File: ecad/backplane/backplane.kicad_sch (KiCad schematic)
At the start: 18 parts, among them J1 10145891-0320J13LF, J2 10145891-0320J13LF, J3 10145891-0320J13LF, J4 10145891-0320J13LF, J6 USB4105-GF-A, U1 MCP16331x-xCH

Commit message: hii
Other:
- moved on the sheet: R3, R4

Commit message: fix backplane pins
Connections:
- net ADDR01 is gone; now on net GND: J1.3, J2.3, J3.3, J4.3
- net ADDR03 is gone; now on net GND: J1.4, J2.4, J3.4, J4.4
- net ADDR05 is gone; now on net BUS05: J1.5, J2.5, J3.5, J4.5
- net ADDR07 is gone; now on net BUS06: J1.6, J2.6, J3.6, J4.6
- net ADDR09 is gone; now on net BUS09: J1.9, J2.9, J3.9, J4.9
- net ADDR10 is gone; now on net 3.3V: J1.49, J2.49, J3.49, J4.49
- net ADDR11 is gone; now on net BUS10: J1.10, J2.10, J3.10, J4.10
- net ADDR12 is gone; now on net 3.3V: J1.50, J2.50, J3.50, J4.50
- net ADDR13 is gone; now on net BUS11: J1.11, J2.11, J3.11, J4.11
- net ADDR14 is gone; now on net GND: J1.51, J2.51, J3.51, J4.51
- net ADDR15 is gone; now on net BUS12: J1.12, J2.12, J3.12, J4.12
- net BUS01 is gone; now on net GND: J1.15, J2.15, J3.15, J4.15
- net BUS03 is gone; now on net GND: J1.16, J2.16, J3.16, J4.16
- net BUS13 is gone; now on net BUS23: J1.23, J2.23, J3.23, J4.23
- net BUS14 is gone; now on net GND: J1.63, J2.63, J3.63, J4.63
- net DATA02 is gone; now on net 3.3V: J1.73, J2.73, J3.73, J4.73
- net DATA04 is gone; now on net 3.3V: J1.74, J2.74, J3.74, J4.74
- net DATA06 is gone; now on net GND: J1.75, J2.75, J3.75, J4.75
- net 3.3V: now also J1.14, J1.2, J1.26, J1.38, J1.61, J1.62, J2.14, J2.2, J2.26, J2.38, J2.61, J2.62, J3.14, J3.2, J3.26, J3.38, J3.61, J3.62, J4.14, J4.2, J4.26, J4.38, J4.61, J4.62; no longer J1.19, J1.31, J1.40, J1.46, J1.52, J1.58, J1.64, J1.7, J1.70, J1.76, J2.19, J2.31, J2.40, J2.46, J2.52, J2.58, J2.64, J2.7, J2.70, J2.76, J3.19, J3.31, J3.40, J3.46, J3.52, J3.58, J3.64, J3.7, J3.70, J3.76, J4.19, J4.31, J4.40, J4.46, J4.52, J4.58, J4.64, J4.7, J4.70, J4.76
- net BUS05: no longer J1.17, J2.17, J3.17, J4.17
- net BUS06: no longer J1.57, J2.57, J3.57, J4.57
- net BUS07: now also J1.7, J2.7, J3.7, J4.7; no longer J1.18, J2.18, J3.18, J4.18
- net BUS08: now also J1.8, J2.8, J3.8, J4.8; no longer J1.60, J2.60, J3.60, J4.60
- net BUS09: no longer J1.21, J2.21, J3.21, J4.21
- net BUS10: no longer J1.61, J2.61, J3.61, J4.61
- net BUS11: no longer J1.22, J2.22, J3.22, J4.22
- net BUS12: no longer J1.62, J2.62, J3.62, J4.62
- net BUS17: now also J1.17, J2.17, J3.17, J4.17; no longer J1.27, J2.27, J3.27, J4.27
- net BUS18: now also J1.18, J2.18, J3.18, J4.18; no longer J1.67, J2.67, J3.67, J4.67
- net BUS19: now also J1.19, J2.19, J3.19, J4.19; no longer J1.28, J2.28, J3.28, J4.28
- net BUS20: now also J1.20, J2.20, J3.20, J4.20; no longer J1.68, J2.68, J3.68, J4.68
- net BUS21: now also J1.21, J2.21, J3.21, J4.21; no longer J1.29, J2.29, J3.29, J4.29
- net BUS22: now also J1.22, J2.22, J3.22, J4.22; no longer J1.69, J2.69, J3.69, J4.69
- net BUS23: no longer J1.30, J2.30, J3.30, J4.30
- net GND: now also J1.27, J1.28, J1.39, J1.40, J1.52, J1.64, J1.76, J2.27, J2.28, J2.39, J2.40, J2.52, J2.64, J2.76, J3.27, J3.28, J3.39, J3.40, J3.52, J3.64, J3.76, J4.27, J4.28, J4.39, J4.40, J4.52, J4.64, J4.76; no longer J1.14, J1.2, J1.20, J1.26, J1.32, J1.38, J1.41, J1.47, J1.53, J1.59, J1.65, J1.71, J1.77, J1.8, J2.14, J2.2, J2.20, J2.26, J2.32, J2.38, J2.41, J2.47, J2.53, J2.59, J2.65, J2.71, J2.77, J2.8, J3.14, J3.2, J3.20, J3.26, J3.32, J3.38, J3.41, J3.47, J3.53, J3.59, J3.65, J3.71, J3.77, J3.8, J4.14, J4.2, J4.20, J4.26, J4.32, J4.38, J4.41, J4.47, J4.53, J4.59, J4.65, J4.71, J4.77, J4.8
- net ADDR00 renamed BUS42
- net ADDR02 renamed BUS43
- net ADDR04 renamed BUS44
- net ADDR06 renamed BUS45
- net ADDR08 renamed BUS48
- net BUS00 renamed BUS54
- net BUS02 renamed BUS55
- net BUS04 renamed BUS56
- net BUS15 renamed BUS24
- net BUS16 renamed BUS66
- net DATA00 renamed BUS72
- net DATA01 renamed BUS33
- net DATA03 renamed BUS34
- net DATA05 renamed BUS35
- net DATA07 renamed BUS36
- new net BUS29: J1.29, J2.29, J3.29, J4.29
- new net BUS30: J1.30, J2.30, J3.30, J4.30
- new net BUS31: J1.31, J2.31, J3.31, J4.31
- new net BUS32: J1.32, J2.32, J3.32, J4.32
- new net BUS41: J1.41, J2.41, J3.41, J4.41
- new net BUS46: J1.46, J2.46, J3.46, J4.46
- new net BUS47: J1.47, J2.47, J3.47, J4.47
- new net BUS53: J1.53, J2.53, J3.53, J4.53
- new net BUS57: J1.57, J2.57, J3.57, J4.57
- new net BUS58: J1.58, J2.58, J3.58, J4.58
- new net BUS59: J1.59, J2.59, J3.59, J4.59
- new net BUS60: J1.60, J2.60, J3.60, J4.60
- new net BUS65: J1.65, J2.65, J3.65, J4.65
- new net BUS67: J1.67, J2.67, J3.67, J4.67
- new net BUS68: J1.68, J2.68, J3.68, J4.68
- new net BUS69: J1.69, J2.69, J3.69, J4.69
- new net BUS70: J1.70, J2.70, J3.70, J4.70
- new net BUS71: J1.71, J2.71, J3.71, J4.71
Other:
- note added: "Buck Converter"

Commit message: more backplane. add nathan's panel changes
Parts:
- added J6: 5017868090, Library:CON_5017868090, symbol Project_Library:5017868090
- added S1: 500SSP1S1M7QEA, Library:SW_500SSP1S1M7QEA, symbol Project_Library:500SSP1S1M7QEA
- renumbered C4 to C1, C5 to C2, C2 to CB1, C1 to Cln_1, C6 to Cln_2, D2 to D1, D1 to DB1, J3 to J2, J6 to J3, J2 to J4, J4 to J5, R3 to R1, R4 to R2, R2 to RBot1, R1 to RTop1
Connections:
- net 3.3V: now also S1.1; no longer C1.1, C2.1, DB1.2 (A), L1.2, RTop1.2
- new net 3.3V IN: C1.1, C2.1, DB1.2 (A), L1.2, RTop1.2, S1.2
- no-connect marks 855 -> 856
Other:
- note added: "Power on"
- note added: "add protection diode"

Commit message: backplane with addr
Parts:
- added R3: 10, Resistor_SMD:R_0402_1005Metric_Pad0.72x0.64mm_HandSolder, symbol Device:R_US
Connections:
- net 3.3V IN: now also R3.2; no longer RTop1.2
- net at J3.A5 (CC1): now also R2.1
- net at J3.B5 (CC2): now also R1.1
- net at J3.B6 (DP2): no longer R2.1
- net at J3.B7 (DN2): no longer R1.1
- net at U1.1 (BOOST): now also CB1.1, DB1.1 (K); no longer CB1.2
- net at D1.1 (K), L1.1, U1.6 (SW): now also CB1.2
- net +5V renamed VBUS
- new net: R3.1, RTop1.2
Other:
- moved on the sheet: CB1

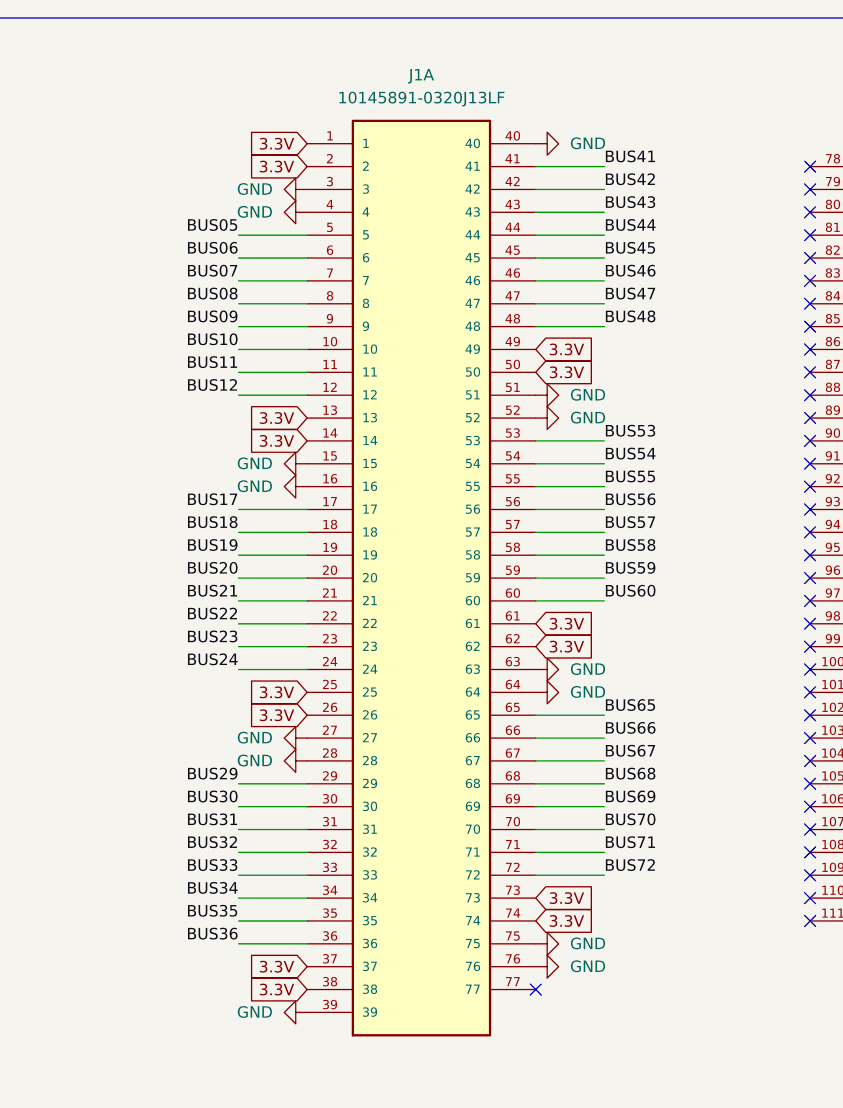
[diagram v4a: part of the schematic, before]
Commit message: backplane with different bus names
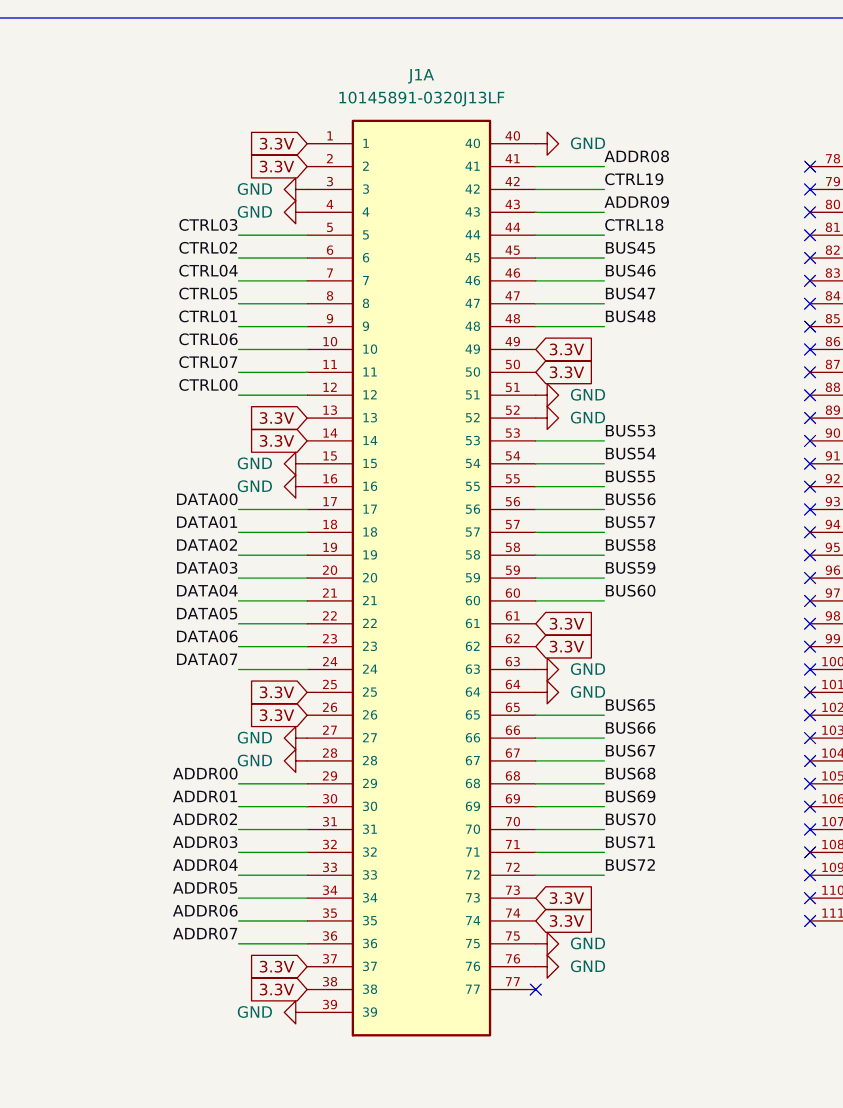
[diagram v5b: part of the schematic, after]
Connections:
- net BUS05: no longer J1.5
- net BUS06: no longer J1.6
- net BUS07: no longer J1.7
- net BUS08: no longer J1.8
- net BUS09: no longer J1.9
- net BUS10: no longer J1.10
- net BUS11: no longer J1.11
- net BUS12: no longer J1.12
- net BUS17: no longer J1.17
- net BUS18: no longer J1.18
- net BUS19: no longer J1.19
- net BUS20: no longer J1.20
- net BUS21: no longer J1.21
- net BUS22: no longer J1.22
- net BUS23: no longer J1.23
- net BUS24: no longer J1.24
- net BUS29: no longer J1.29
- net BUS30: no longer J1.30
- net BUS31: no longer J1.31
- net BUS32: no longer J1.32
- net BUS33: no longer J1.33
- net BUS34: no longer J1.34
- net BUS35: no longer J1.35
- net BUS36: no longer J1.36
- net BUS41: no longer J1.41
- net BUS42: no longer J1.42
- net BUS43: no longer J1.43
- net BUS44: no longer J1.44
- new net ADDR00: J1.29
- new net ADDR01: J1.30
- new net ADDR02: J1.31
- new net ADDR03: J1.32
- new net ADDR04: J1.33
- new net ADDR05: J1.34
- new net ADDR06: J1.35
- new net ADDR07: J1.36
- new net ADDR08: J1.41
- new net ADDR09: J1.43
- new net CTRL00: J1.12
- new net CTRL01: J1.9
- new net CTRL02: J1.6
- new net CTRL03: J1.5
- new net CTRL04: J1.7
- new net CTRL05: J1.8
- new net CTRL06: J1.10
- new net CTRL07: J1.11
- new net CTRL18: J1.44
- new net CTRL19: J1.42
- new net DATA00: J1.17
- new net DATA01: J1.18
- new net DATA02: J1.19
- new net DATA03: J1.20
- new net DATA04: J1.21
- new net DATA05: J1.22
- new net DATA06: J1.23
- new net DATA07: J1.24
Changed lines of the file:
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@@
 		)
 	)
-	(label "BUS18"
+	(label "DATA01"
 		(at 43.18 76.2 180)
 		(effects
@@
 		)
 	)
-	(label "BUS19"
+	(label "DATA02"
 		(at 43.18 78.74 180)
 		(effects
@@
 		)
 	)
-	(label "BUS07"
+	(label "CTRL04"
 		(at 43.18 48.26 180)
 		(effects
@@
 		)
 	)
-	(label "BUS20"
+	(label "DATA03"
 		(at 43.18 81.28 180)
 		(effects
@@
 		)
 	)
-	(label "BUS22"
+	(label "DATA05"
 		(at 43.18 86.36 180)
 		(effects
@@
 		)
 	)
-	(label "BUS30"
+	(label "ADDR01"
 		(at 43.18 106.68 180)
 		(effects
@@
 		)
 	)
-	(label "BUS29"
+	(label "ADDR00"
 		(at 43.18 104.14 180)
 		(effects
@@
 		)
 	)
-	(label "BUS41"
+	(label "ADDR08"
 		(at 83.82 35.56 0)
 		(effects
@@
 		)
 	)
-	(label "BUS43"
+	(label "ADDR09"
 		(at 83.82 40.64 0)
 		(effects
@@
 		)
 	)
-	(label "BUS11"
+	(label "CTRL07"
 		(at 43.18 58.42 180)
 		(effects
@@
 		)
 	)
-	(label "BUS21"
+	(label "DATA04"
 		(at 43.18 83.82 180)
 		(effects
@@
 		)
 	)
-	(label "BUS31"
+	(label "ADDR02"
 		(at 43.18 109.22 180)
 		(effects
@@
 		)
 	)
-	(label "BUS17"
+	(label "DATA00"
 		(at 43.18 73.66 180)
 		(effects
@@
 		)
 	)
-	(label "BUS24"
+	(label "DATA07"
 		(at 43.18 91.44 180)
 		(effects
@@
 		)
 	)
-	(label "BUS35"
+	(label "ADDR06"
 		(at 43.18 119.38 180)
 		(effects
@@
 		)
 	)
-	(label "BUS10"
+	(label "CTRL06"
 		(at 43.18 55.88 180)
 		(effects
@@
 		)
 	)
-	(label "BUS44"
+	(label "CTRL18"
 		(at 83.82 43.18 0)
 		(effects
@@
 		)
 	)
-	(label "BUS36"
+	(label "ADDR07"
 		(at 43.18 121.92 180)
 		(effects
@@
 		)
 	)
-	(label "BUS08"
+	(label "CTRL05"
 		(at 43.18 50.8 180)
 		(effects
@@
 		)
 	)
-	(label "BUS06"
+	(label "CTRL02"
 		(at 43.18 45.72 180)
 		(effects
@@
 		)
 	)
-	(label "BUS33"
+	(label "ADDR04"
 		(at 43.18 114.3 180)
 		(effects
@@
 		)
 	)
-	(label "BUS34"
+	(label "ADDR05"
 		(at 43.18 116.84 180)
 		(effects
@@
 		)
 	)
-	(label "BUS09"
+	(label "CTRL01"
 		(at 43.18 53.34 180)
 		(effects
@@
 		)
 	)
-	(label "BUS23"
+	(label "DATA06"
 		(at 43.18 88.9 180)
 		(effects
@@
 		)
 	)
-	(label "BUS12"
+	(label "CTRL00"
 		(at 43.18 60.96 180)
 		(effects
@@
 		)
 	)
-	(label "BUS42"
+	(label "CTRL19"
 		(at 83.82 38.1 0)
 		(effects
@@
 		)
 	)
-	(label "BUS32"
+	(label "ADDR03"
 		(at 43.18 111.76 180)
 		(effects
@@
 		)
 	)
-	(label "BUS05"
+	(label "CTRL03"
 		(at 43.18 43.18 180)
 		(effects
